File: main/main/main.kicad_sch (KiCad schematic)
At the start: 1 part, among them U1 Teensy4.1

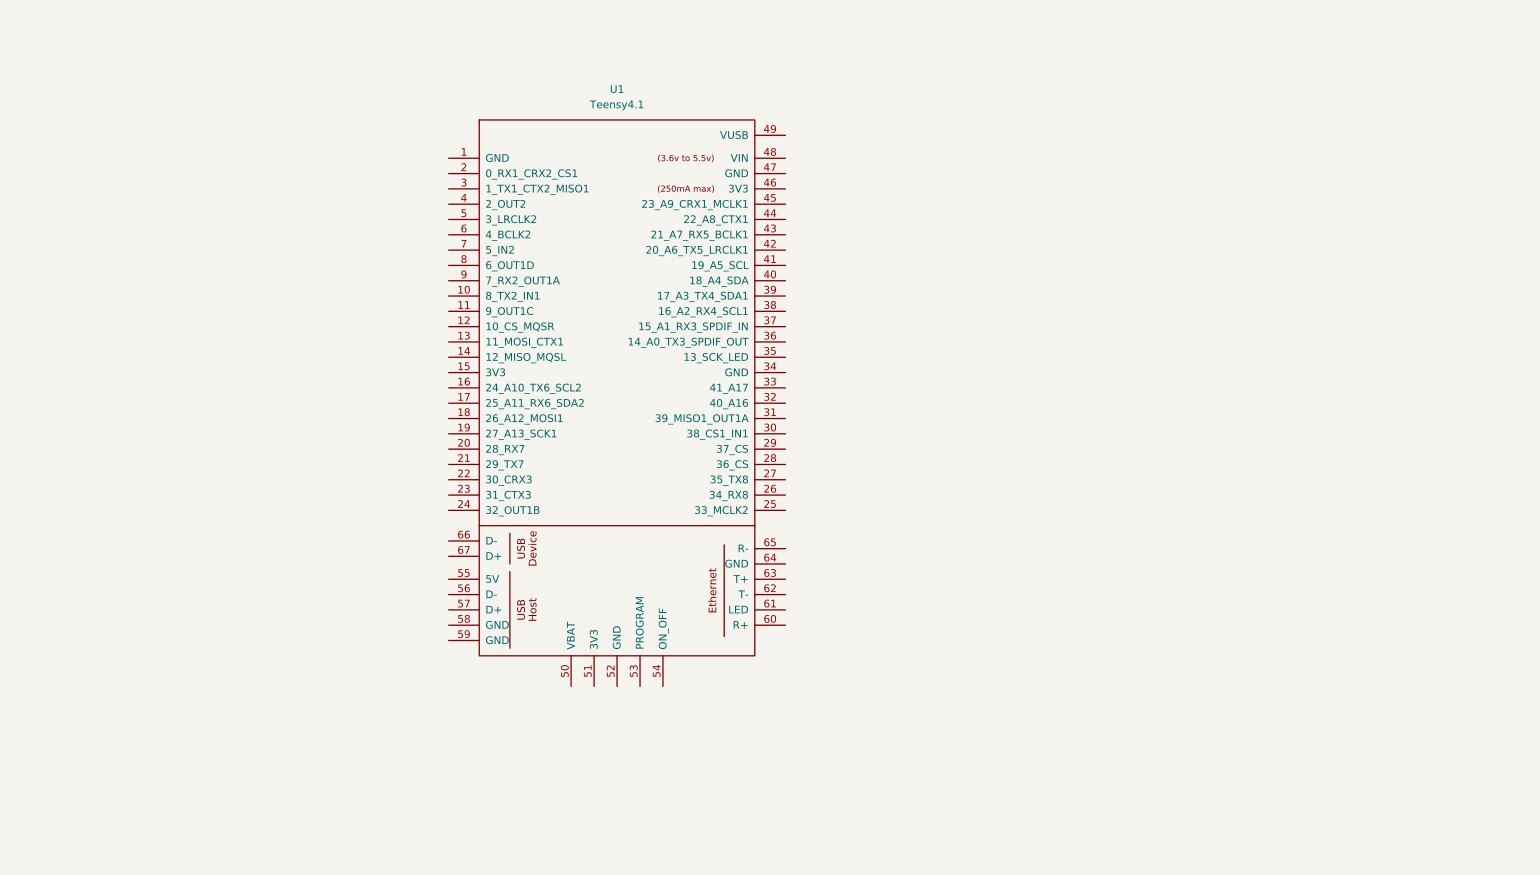
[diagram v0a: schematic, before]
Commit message: working on main pcb (teensy, plugs, encoder traces)
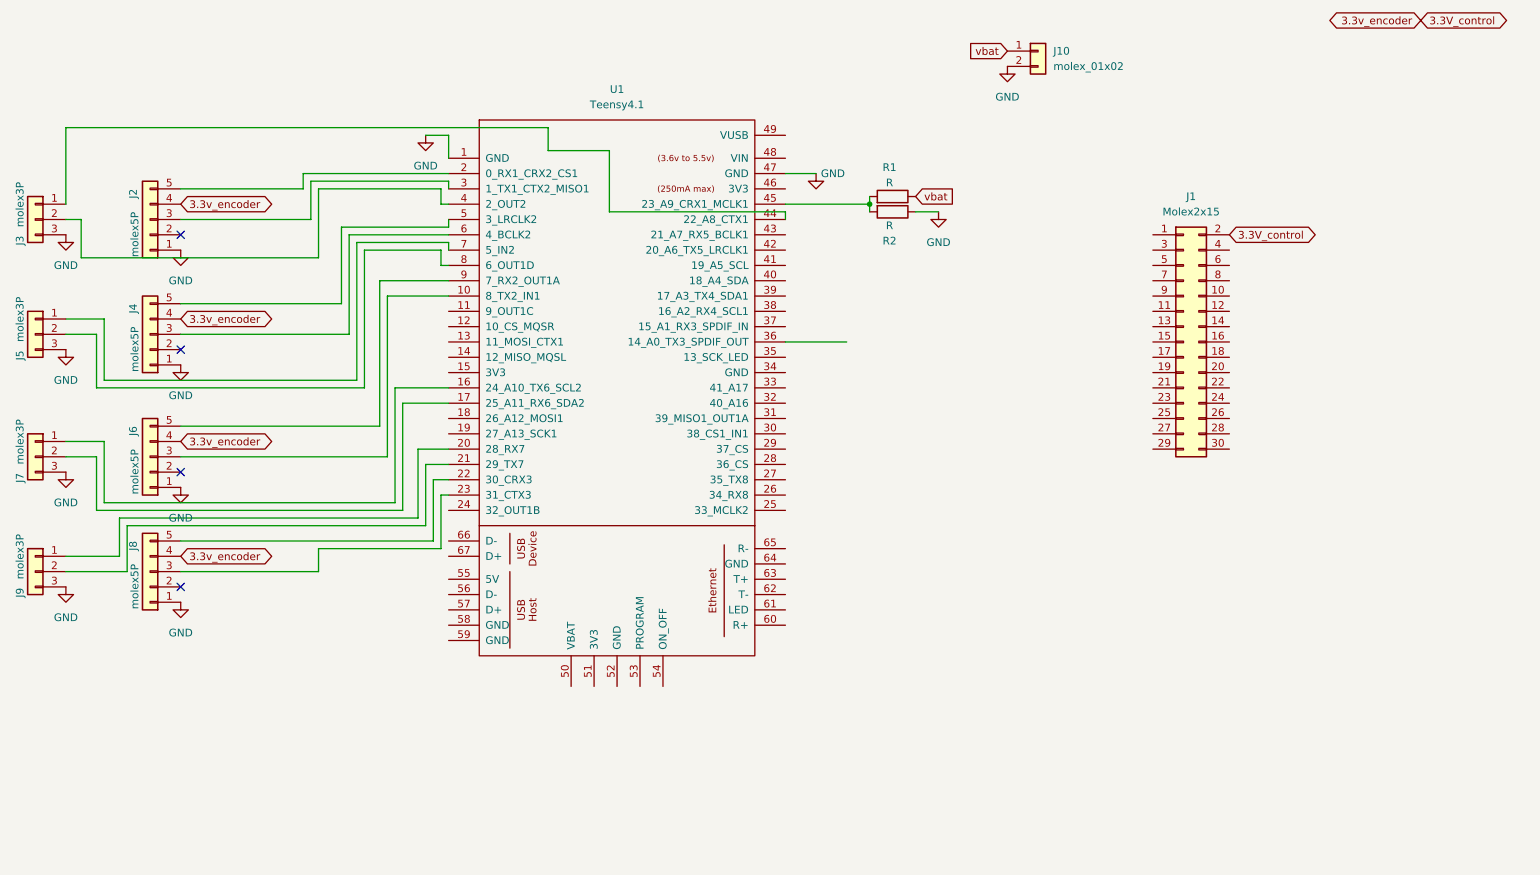
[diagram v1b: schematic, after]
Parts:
- added J1: Molex2x15, projlib:CON_702463001_MOL_molex2x15, symbol projlib:molex_02x15_Odd_Even
- added J10: molex_01x02, projlib:Molex_SL_171971-0002_1x02_P2.54mm_Vertical, symbol projlib:molex_01x02
- added J2, J4, J6, J8: molex5P, projlib:Molex_SL_171971-0005_1x05_P2.54mm_Vertical, symbol Connector_Generic:Conn_01x05
- added J3, J5, J7, J9: molex3P, projlib:Molex_SL_171971-0003_1x03_P2.54mm_Vertical, symbol Connector_Generic:Conn_01x03
- added R1, R2: R, Resistor_THT:R_Axial_DIN0207_L6.3mm_D2.5mm_P10.16mm_Horizontal, symbol Device:R
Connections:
- net GND: now reaches U1.1 (GND)
- net GND: now also U1.47 (GND), J10.2 (Pin_2), J2.1 (Pin_1), J3.3 (Pin_3), J4.1 (Pin_1), J5.3 (Pin_3), J6.1 (Pin_1), J7.3 (Pin_3), J8.1 (Pin_1), J9.3 (Pin_3), R2.1
- net at U1.10 (8_TX2_IN1): now also J6.3 (Pin_3)
- net at U1.16 (24_A10_TX6_SCL2): now also J7.1 (Pin_1)
- net at U1.17 (25_A11_RX6_SDA2): now also J7.2 (Pin_2)
- net at U1.2 (0_RX1_CRX2_CS1): now also J2.5 (Pin_5)
- net at U1.20 (28_RX7): now also J9.1 (Pin_1)
- net at U1.21 (29_TX7): now also J9.2 (Pin_2)
- net at U1.22 (30_CRX3): now also J8.5 (Pin_5)
- net at U1.23 (31_CTX3): now also J8.3 (Pin_3)
- net at U1.3 (1_TX1_CTX2_MISO1): now also J2.3 (Pin_3)
- net at U1.4 (2_OUT2): now also J3.2 (Pin_2)
- net at U1.44 (22_A8_CTX1): now also J3.1 (Pin_1)
- net at U1.45 (23_A9_CRX1_MCLK1): now also R1.2, R2.2
- net at U1.5 (3_LRCLK2): now also J4.5 (Pin_5)
- net at U1.6 (4_BCLK2): now also J4.3 (Pin_3)
- net at U1.7 (5_IN2): now also J5.1 (Pin_1)
- net at U1.8 (6_OUT1D): now also J5.2 (Pin_2)
- net at U1.9 (7_RX2_OUT1A): now also J6.5 (Pin_5)
- new net 3.3V_control: J1.2 (Pin_2), J2.4 (Pin_4), J4.4 (Pin_4), J6.4 (Pin_4), J8.4 (Pin_4)
- new net vbat: J10.1 (Pin_1), R1.1
- no-connect marks 0 -> 4

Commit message: working on control pcb
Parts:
- added U2: ~, projlib:pololu4085, symbol projlib:pololu4085 5v
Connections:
- net GND: now also J1.1 (Pin_1), U2.2 (gnd)
- net vbat: now also J1.2 (Pin_2), U2.3 (vin)
- net at R1.2, R2.2: now also U1.30 (38_CS1_IN1); no longer U1.45 (23_A9_CRX1_MCLK1)
- net 3.3v_encoder: now reaches U1.46 (3V3)
- net 3.3v_encoder: now also J2.4 (Pin_4), J4.4 (Pin_4), J6.4 (Pin_4), J8.4 (Pin_4)
- net at U1.48 (VIN): now also U2.1 (5v)
- removed net 3.3V_control: J1.2 (Pin_2), J2.4 (Pin_4), J4.4 (Pin_4), J6.4 (Pin_4), J8.4 (Pin_4)

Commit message: add joystick plug, adjust resistors
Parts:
- added J11: Conn_01x04, projlib:Molex_SL_171971-0004_1x04_P2.54mm_Vertical, symbol Connector_Generic:Conn_01x04
- R1, R2: footprint Resistor_THT:R_Axial_DIN0207_L6.3mm_D2.5mm_P10.16mm_Horizontal -> Resistor_THT:R_Axial_DIN0204_L3.6mm_D1.6mm_P5.08mm_Horizontal
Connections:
- net 3.3v_encoder: now also J11.2 (Pin_2)
- net GND: now also J11.1 (Pin_1)
- net at U1.18 (26_A12_MOSI1): now also J11.4 (Pin_4)
- net at U1.19 (27_A13_SCK1): now also J11.3 (Pin_3)
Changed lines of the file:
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@@
+	(wire
+		(pts
+			(xy 91.44 128.27) (xy 90.17 128.27)
+		)
+		(stroke
+			(width 0)
+			(type default)
+		)
+	)
 	(wire
 		(pts
@@
 	(wire
 		(pts
+			(xy 90.17 123.19) (xy 92.71 123.19)
+		)
+		(stroke
+			(width 0)
+			(type default)
+		)
+	)
+	(wire
+		(pts
 			(xy 162.56 43.18) (xy 175.26 43.18)
 		)
@@
 	(wire
 		(pts
+			(xy 106.68 86.36) (xy 91.44 86.36)
+		)
+		(stroke
+			(width 0)
+			(type default)
+		)
+	)
+	(wire
+		(pts
 			(xy 106.68 57.15) (xy 106.68 58.42)
 		)
@@
 	(wire
 		(pts
+			(xy 91.44 86.36) (xy 91.44 120.65)
+		)
+		(stroke
+			(width 0)
+			(type default)
+		)
+	)
+	(wire
+		(pts
 			(xy 92.71 58.42) (xy 105.41 58.42)
 		)
@@
 	(wire
 		(pts
+			(xy 106.68 88.9) (xy 92.71 88.9)
+		)
+		(stroke
+			(width 0)
+			(type default)
+		)
+	)
+	(wire
+		(pts
 			(xy 166.37 48.26) (xy 166.37 50.8)
 		)
@@
 	(wire
 		(pts
+			(xy 91.44 120.65) (xy 90.17 120.65)
+		)
+		(stroke
+			(width 0)
+			(type default)
+		)
+	)
+	(wire
+		(pts
 			(xy 123.19 38.1) (xy 43.18 38.1)
 		)
@@
 		(pts
 			(xy 48.26 72.39) (xy 48.26 81.28)
+		)
+		(stroke
+			(width 0)
+			(type default)
+		)
+	)
+	(wire
+		(pts
+			(xy 92.71 88.9) (xy 92.71 123.19)
 		)
 		(stroke
@@
 				)
 				(justify right)
+				(hide yes)
+			)
+		)
+	)
+	(global_label "3.3v_encoder"
+		(shape bidirectional)
+		(at 90.17 125.73 0)
+		(fields_autoplaced yes)
+		(effects
+			(font
+				(size 1.27 1.27)
+			)
+			(justify left)
+		)
+		(property "Intersheetrefs" "${INTERSHEET_REFS}"
+			(at 106.7245 125.73 0)
+			(effects
+				(font
+					(size 1.27 1.27)
+				)
+				(justify left)
 				(hide yes)
 			)
@@
 			)
 		)
-		(property "Datasheet" ""
+		(property "Datasheet" "https://www.pjrc.com/store/teensy41.html"
 			(at 124.46 87.63 0)
 			(effects
@@
 	)
 	(symbol
+		(lib_id "Connector_Generic:Conn_01x04")
+		(at 85.09 125.73 180)
+		(unit 1)
+		(exclude_from_sim no)
+		(in_bom yes)
+		(on_board yes)
+		(dnp no)
+		(fields_autoplaced yes)
+		(property "Reference" "J11"
+			(at 85.09 114.3 0)
+			(effects
+				(font
+					(size 1.27 1.27)
+				)
+			)
+		)
+		(property "Value" "Conn_01x04"
+			(at 85.09 116.84 0)
+			(effects
+				(font
+					(size 1.27 1.27)
+				)
+			)
+		)
+		(property "Footprint" "projlib:Molex_SL_171971-0004_1x04_P2.54mm_Vertical"
+			(at 85.09 125.73 0)
+			(effects
+				(font
+					(size 1.27 1.27)
+				)
+				(hide yes)
+			)
+		)
+		(property "Datasheet" "~"
+			(at 85.09 125.73 0)
+			(effects
+				(font
+					(size 1.27 1.27)
+				)
+				(hide yes)
+			)
+		)
+		(property "Description" "Generic connector, single row, 01x04, script generated (kicad-library-utils/schlib/autogen/connector/)"
+			(at 85.09 125.73 0)
+			(effects
+				(font
+					(size 1.27 1.27)
+				)
+				(hide yes)
+			)
+		)
+		(pin "1"
+		)
+		(pin "2"
+		)
+		(pin "4"
+		)
+		(pin "3"
+		)
+		(instances
+			(project ""
+				(path "/ab47a88c-4e7b-4d2a-8992-259f4c293a97"
+					(reference "J11")
+					(unit 1)
+				)
+			)
+		)
+	)
+	(symbol
 		(lib_id "projlib:pololu4085 5v")
 		(at 177.8 34.29 0)
@@
 			)
 		)
-		(property "Footprint" "Resistor_THT:R_Axial_DIN0207_L6.3mm_D2.5mm_P10.16mm_Horizontal"
+		(property "Footprint" "Resistor_THT:R_Axial_DIN0204_L3.6mm_D1.6mm_P5.08mm_Horizontal"
 			(at 180.34 89.408 90)
 			(effects
@@
 			)
 		)
-		(property "Footprint" "Resistor_THT:R_Axial_DIN0207_L6.3mm_D2.5mm_P10.16mm_Horizontal"
+		(property "Footprint" "Resistor_THT:R_Axial_DIN0204_L3.6mm_D1.6mm_P5.08mm_Horizontal"
 			(at 180.34 88.392 90)
 			(effects
@@
 					(unit 1)
 				)
+			)
+		)
+	)
+	(symbol
+		(lib_id "power:GND")
+		(at 91.44 128.27 0)
+		(unit 1)
+		(exclude_from_sim no)
+		(in_bom yes)
+		(on_board yes)
+		(dnp no)
+		(fields_autoplaced yes)
+		(property "Reference" "#PWR015"
+			(at 91.44 134.62 0)
+			(effects
+				(font
+					(size 1.27 1.27)
+				)
+				(hide yes)
+			)
+		)
+		(property "Value" "GND"
+			(at 91.44 133.35 0)
+			(effects
+				(font
+					(size 1.27 1.27)
+				)
+			)
+		)
+		(property "Footprint" ""
+			(at 91.44 128.27 0)
+			(effects
+				(font
+					(size 1.27 1.27)
+				)
+				(hide yes)
+			)
+		)
+		(property "Datasheet" ""
+			(at 91.44 128.27 0)
+			(effects
+				(font
+					(size 1.27 1.27)
+				)
+				(hide yes)
+			)
+		)
+		(property "Description" "Power symbol creates a global label with name \"GND\" , ground"
+			(at 91.44 128.27 0)
+			(effects
+				(font
+					(size 1.27 1.27)
+				)
+				(hide yes)
+			)
+		)
+		(pin "1"
+		)
+		(instances
+			(project "main"
+				(path "/ab47a88c-4e7b-4d2a-8992-259f4c293a97"
+					(reference "#PWR015")
+					(unit 1)
+				)

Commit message: control pcb almost done
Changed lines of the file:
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@@
+	(wire
+		(pts
+			(xy 127 152.4) (xy 154.94 152.4)
+		)
+		(stroke
+			(width 0)
+			(type default)
+		)
+	)
 	(wire
 		(pts
@@
 	(wire
 		(pts
+			(xy 115.57 142.24) (xy 115.57 160.02)
+		)
+		(stroke
+			(width 0)
+			(type default)
+		)
+	)
+	(wire
+		(pts
 			(xy 43.18 38.1) (xy 43.18 50.8)
 		)
@@
 	(wire
 		(pts
+			(xy 115.57 160.02) (xy 143.51 160.02)
+		)
+		(stroke
+			(width 0)
+			(type default)
+		)
+	)
+	(wire
+		(pts
 			(xy 85.09 111.76) (xy 62.23 111.76)
 		)
@@
 	(wire
 		(pts
+			(xy 127 130.81) (xy 127 152.4)
+		)
+		(stroke
+			(width 0)
+			(type default)
+		)
+	)
+	(wire
+		(pts
 			(xy 88.9 54.61) (xy 88.9 67.31)
 		)
@@
 	(wire
 		(pts
+			(xy 143.51 137.16) (xy 143.51 160.02)
+		)
+		(stroke
+			(width 0)
+			(type default)
+		)
+	)
+	(wire
+		(pts
 			(xy 90.17 55.88) (xy 90.17 72.39)
 		)
@@
 	(wire
 		(pts
+			(xy 154.94 142.24) (xy 115.57 142.24)
+		)
+		(stroke
+			(width 0)
+			(type default)
+		)
+	)
+	(wire
+		(pts
 			(xy 92.71 81.28) (xy 92.71 58.42)
 		)
@@
 		)
 		(stroke
+			(width 0)
+			(type default)
+		)
+	)
+	(wire
+		(pts
+			(xy 154.94 152.4) (xy 154.94 142.24)
+		)
+		(stroke

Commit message: main fully routed
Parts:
- added BT1: Battery_Cell, TestPoint:TestPoint_2Pads_Pitch2.54mm_Drill0.8mm, symbol Device:Battery_Cell
- added J12: Conn_02x03, Connector_PinHeader_2.54mm:PinHeader_2x03_P2.54mm_Horizontal, symbol Connector_Generic:Conn_01x06
- added TP1: TestPoint, TestPoint:TestPoint_2Pads_Pitch2.54mm_Drill0.8mm, symbol Connector:TestPoint_2Pole
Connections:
- net 3.3v_encoder: now also U1.15 (3V3); no longer U1.46 (3V3)
- net GND: now also U1.34 (GND), TP1.2
- net vbat: now also J1.26 (Pin_26)
- net at U1.11 (9_OUT1C): now also J3.1 (Pin_1)
- net at U1.12 (10_CS_MQSR): now also J1.16 (Pin_16)
- net at U1.13 (11_MOSI_CTX1): now also J1.18 (Pin_18)
- net at U1.14 (12_MISO_MQSL): now also J1.20 (Pin_20)
- net at U1.20 (28_RX7): now also TP1.1; no longer J9.1 (Pin_1)
- net at U1.24 (32_OUT1B): now also J9.1 (Pin_1)
- net at U1.25 (33_MCLK2): now also J1.28 (Pin_28)
- net at U1.26 (34_RX8): now also J1.27 (Pin_27)
- net at U1.27 (35_TX8): now also J1.25 (Pin_25)
- net at U1.28 (36_CS): now also J1.30 (Pin_30)
- net at U1.29 (37_CS): now also J1.29 (Pin_29)
- net at U1.31 (39_MISO1_OUT1A): now also J1.24 (Pin_24)
- net at U1.32 (40_A16): now also J1.23 (Pin_23)
- net at U1.33 (41_A17): now also J1.22 (Pin_22)
- net at U1.36 (14_A0_TX3_SPDIF_OUT): now also J1.21 (Pin_21)
- net at U1.37 (15_A1_RX3_SPDIF_IN): now also J1.19 (Pin_19)
- net at U1.38 (16_A2_RX4_SCL1): now also J1.17 (Pin_17)
- net at U1.39 (17_A3_TX4_SDA1): now also J1.15 (Pin_15)
- net at U1.40 (18_A4_SDA): now also J1.13 (Pin_13)
- net at U1.41 (19_A5_SCL): now also J1.14 (Pin_14)
- net at U1.42 (20_A6_TX5_LRCLK1): now also J1.12 (Pin_12)
- net at U1.43 (21_A7_RX5_BCLK1): now also J1.10 (Pin_10)
- net at U1.44 (22_A8_CTX1): now also J1.8 (Pin_8); no longer J3.1 (Pin_1)
- net at U1.45 (23_A9_CRX1_MCLK1): now also J1.6 (Pin_6)
- net at U1.50 (VBAT): now also BT1.1 (+)
- net at U1.52 (GND): now also BT1.2 (-)
- net at J1.11 (Pin_11): now also J12.6 (Pin_6)
- net at J1.3 (Pin_3): now also J12.3 (Pin_3)
- net at J1.4 (Pin_4): now also J12.5 (Pin_5)
- net at J1.5 (Pin_5): now also J12.1 (Pin_1)
- net at J1.7 (Pin_7): now also J12.2 (Pin_2)
- net at J1.9 (Pin_9): now also J12.4 (Pin_4)
- no-connect marks 4 -> 14

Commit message: change plug for extra pns
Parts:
- removed J12: Conn_02x03, Connector_PinHeader_2.54mm:PinHeader_2x03_P2.54mm_Horizontal, symbol Connector_Generic:Conn_01x06
- added J12: Conn_01x08, projlib:PinSocket_2x04_P1.27mm_Vertical, symbol Connector_Generic:Conn_01x08
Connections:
- net GND: now also BT1.2 (-), U1.52 (GND), U1.58 (GND), U1.59 (GND)
- net at U1.12 (10_CS_MQSR): now also J1.8 (Pin_8); no longer J1.16 (Pin_16)
- net at U1.13 (11_MOSI_CTX1): now also J1.11 (Pin_11); no longer J1.18 (Pin_18)
- net at U1.14 (12_MISO_MQSL): now also J1.13 (Pin_13); no longer J1.20 (Pin_20)
- net at U1.31 (39_MISO1_OUT1A): now also J1.23 (Pin_23); no longer J1.24 (Pin_24)
- net at U1.32 (40_A16): now also J1.20 (Pin_20); no longer J1.23 (Pin_23)
- net at U1.33 (41_A17): now also J1.19 (Pin_19); no longer J1.22 (Pin_22)
- net at U1.36 (14_A0_TX3_SPDIF_OUT): now also J1.16 (Pin_16); no longer J1.21 (Pin_21)
- net at U1.37 (15_A1_RX3_SPDIF_IN): now also J1.14 (Pin_14); no longer J1.19 (Pin_19)
- net at U1.38 (16_A2_RX4_SCL1): now also J1.12 (Pin_12); no longer J1.17 (Pin_17)
- net at U1.39 (17_A3_TX4_SDA1): now also J1.10 (Pin_10); no longer J1.15 (Pin_15)
- net at U1.40 (18_A4_SDA): now also J1.9 (Pin_9); no longer J1.13 (Pin_13)
- net at U1.41 (19_A5_SCL): now also J1.7 (Pin_7); no longer J1.14 (Pin_14)
- net at U1.42 (20_A6_TX5_LRCLK1): now also J1.6 (Pin_6); no longer J1.12 (Pin_12)
- net at U1.43 (21_A7_RX5_BCLK1): now also J1.5 (Pin_5); no longer J1.10 (Pin_10)
- net at U1.44 (22_A8_CTX1): now also J1.4 (Pin_4); no longer J1.8 (Pin_8)
- net at U1.45 (23_A9_CRX1_MCLK1): now also J1.3 (Pin_3); no longer J1.6 (Pin_6)
- new net: J1.21 (Pin_21), J12.1 (Pin_1)
- new net: J1.22 (Pin_22), J12.3 (Pin_3)
- new net: J1.18 (Pin_18), J12.4 (Pin_4)
- new net: J1.24 (Pin_24), J12.5 (Pin_5)
- new net: J1.17 (Pin_17), J12.6 (Pin_6)
- new net: J1.15 (Pin_15), J12.8 (Pin_8)
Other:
- note added: "49"
- note added: "50"
- note added: "51"
- note added: "52"
- note added: "53"
- note added: "54"

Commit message: final adjustments for v1.0
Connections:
- net at U1.10 (8_TX2_IN1): now also J6.5 (Pin_5); no longer J6.3 (Pin_3)
- net at U1.9 (7_RX2_OUT1A): now also J6.3 (Pin_3); no longer J6.5 (Pin_5)
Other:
- company: (none) -> PNW Assistive Technology
- title: (none) -> main PCB for standing frame
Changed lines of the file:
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@@
 	(generator "eeschema")
 	(generator_version "8.0")
-	(paper "A4")
+	(paper "USLetter")
+	(title_block
+		(title "main PCB for standing frame")
+		(date "2024-07-10")
+		(rev "v1.0")
+		(company "PNW Assistive Technology")
+		(comment 1 "Joshua Phelps")
+	)
 	(junction
 		(at 176.53 88.9)
@@
 	(wire
 		(pts
-			(xy 106.68 63.5) (xy 95.25 63.5)
+			(xy 106.68 63.5) (xy 96.52 63.5)
 		)
 		(stroke
@@
 	(wire
 		(pts
-			(xy 95.25 63.5) (xy 95.25 87.63)
-		)
-		(stroke
-			(width 0)
-			(type default)
-		)
-	)
-	(wire
-		(pts
 			(xy 91.44 57.15) (xy 106.68 57.15)
 		)
@@
 	(wire
 		(pts
-			(xy 105.41 77.47) (xy 106.68 77.47)
+			(xy 127 77.47) (xy 106.68 77.47)
 		)
 		(stroke
@@
 	(wire
 		(pts
-			(xy 96.52 66.04) (xy 106.68 66.04)
+			(xy 95.25 66.04) (xy 106.68 66.04)
 		)
 		(stroke
@@
 	(wire
 		(pts
+			(xy 95.25 66.04) (xy 95.25 87.63)
+		)
+		(stroke
+			(width 0)
+			(type default)
+		)
+	)
+	(wire
+		(pts
 			(xy 97.79 81.28) (xy 106.68 81.28)
 		)
@@
 	(wire
 		(pts
-			(xy 96.52 92.71) (xy 96.52 66.04)
+			(xy 96.52 63.5) (xy 96.52 92.71)
 		)
 		(stroke
@@
 	(global_label "3.3v_encoder"
 		(shape bidirectional)
-		(at 105.41 77.47 180)
+		(at 127 77.47 0)
 		(fields_autoplaced yes)
 		(effects
@@
 				(size 1.27 1.27)
 			)
-			(justify right)
+			(justify left)
 		)
 		(property "Intersheetrefs" "${INTERSHEET_REFS}"
-			(at 88.8555 77.47 0)
+			(at 143.5545 77.47 0)
 			(effects
 				(font
 					(size 1.27 1.27)
 				)
-				(justify right)
+				(justify left)
 				(hide yes)
 			)
